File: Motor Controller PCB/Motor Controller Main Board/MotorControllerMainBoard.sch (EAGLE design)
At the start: 26 parts, among them T1 TEENSY_3.1_ALL_PINS

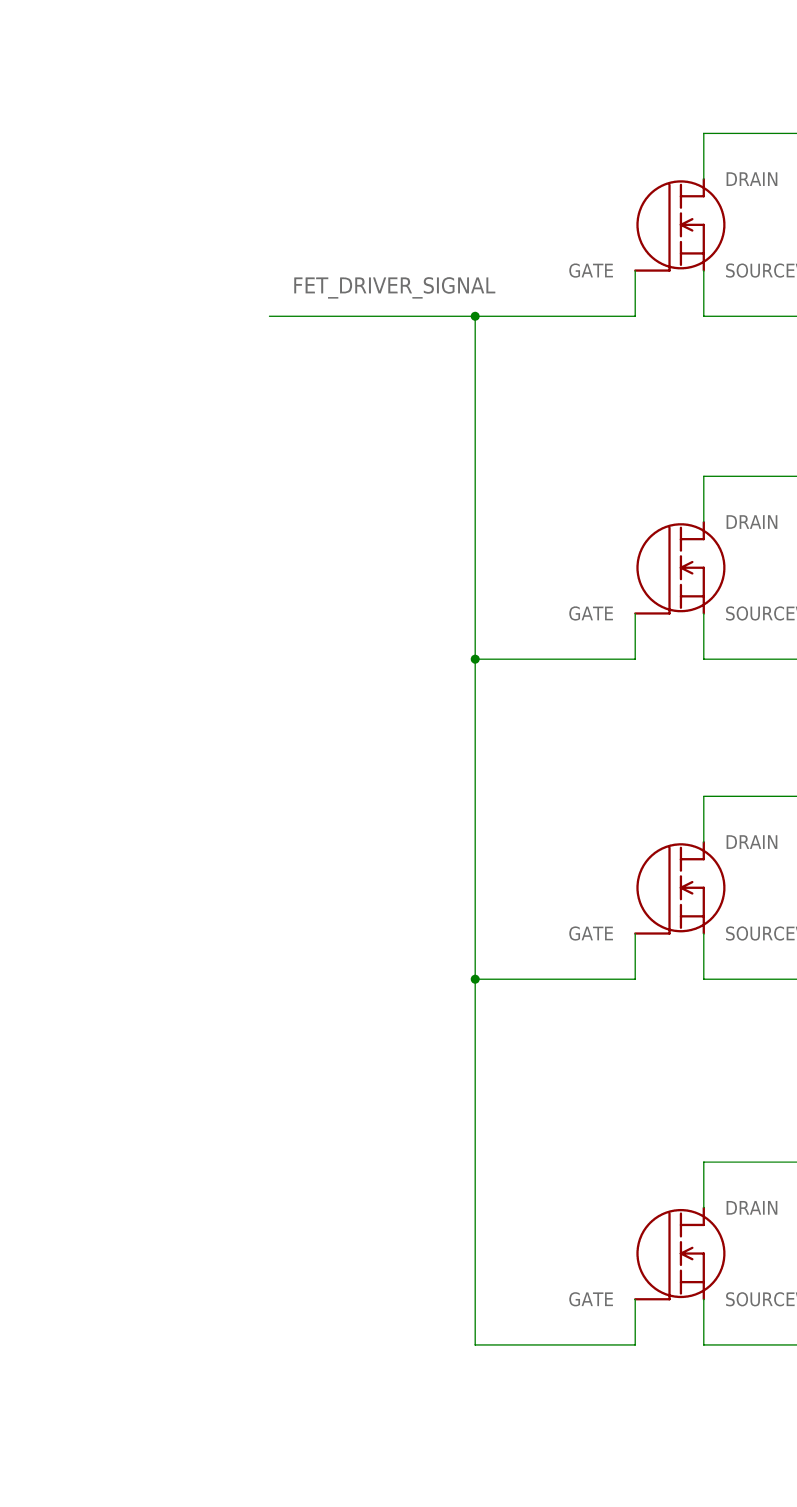
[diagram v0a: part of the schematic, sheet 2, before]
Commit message: Modified the mosfet network
added headers to enable/disable individual fets

also we're going to drive the fets with 12V instead of 15V.
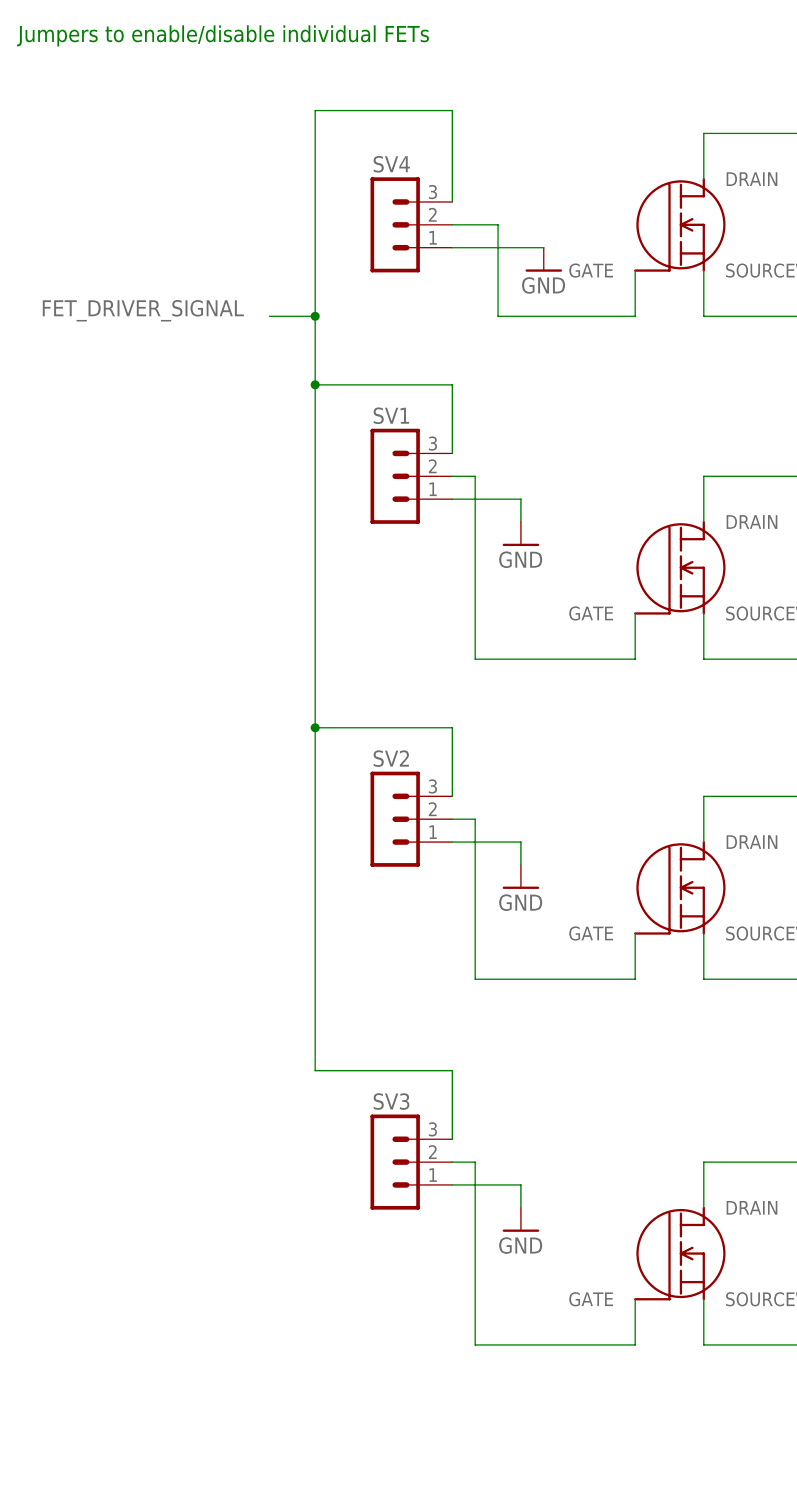
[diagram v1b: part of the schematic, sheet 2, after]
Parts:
- added SV1, SV2, SV3, SV4: (no value), con-lstb:MA03-1
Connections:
- net 15V_POWER_REGULATED renamed 12V_POWER_REGULATED
- new net N$3: SV1.2, U$2.GATE
- new net N$5: SV3.2, U$4.GATE
- new net N$8: SV4.2, U$1.GATE
- net FET_DRIVER_SIGNAL: now also SV1.3, SV2.2, SV2.3, SV3.3, SV4.3; no longer U$1.GATE, U$2.GATE, U$4.GATE
- net GND: now also SV1.1, SV2.1, SV3.1
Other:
- note added: "12V Variable Supply"
- note added: "Jumpers to enable/disable individual FETs"
- note removed: "15V Variable Supply"
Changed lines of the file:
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@@
 <?xml version="1.0" encoding="utf-8"?>
 <!DOCTYPE eagle SYSTEM "eagle.dtd">
-<eagle version="7.7.0">
+<eagle version="7.5.0">
 <drawing>
 <settings>
@@
 <part name="C12" library="MotorControllerEagleLibrary" deviceset="EEUFR1H221B" device=""/>
 <part name="U$13" library="MotorControllerEagleLibrary" deviceset="TL2575-05IKTTR" device=""/>
+<part name="SV1" library="con-lstb" deviceset="MA03-1" device=""/>
+<part name="SV2" library="con-lstb" deviceset="MA03-1" device=""/>
+<part name="SV3" library="con-lstb" deviceset="MA03-1" device=""/>
+<part name="GND5" library="E-P-008-R1.2" deviceset="GND" device=""/>
+<part name="GND6" library="E-P-008-R1.2" deviceset="GND" device=""/>
+<part name="GND7" library="E-P-008-R1.2" deviceset="GND" device=""/>
+<part name="SV4" library="con-lstb" deviceset="MA03-1" device=""/>
+<part name="GND8" library="E-P-008-R1.2" deviceset="GND" device=""/>
 </parts>
 <sheets>
@@
 </segment>
 </net>
-<net name="15V_POWER_REGULATED" class="0">
+<net name="12V_POWER_REGULATED" class="0">
 <segment>
 <wire x1="96.52" y1="66.04" x2="96.52" y2="58.42" width="0.1524" layer="91"/>
@@
 <plain>
 <text x="180.34" y="27.94" size="5.08" layer="94">POWER MOSFETS</text>
+<text x="63.5" y="195.58" size="1.778" layer="91">Jumpers to enable/disable individual FETs</text>
 </plain>
 <instances>
@@
 <instance part="U$4" gate="G$1" x="137.16" y="60.96"/>
 <instance part="GND2" gate="1" x="187.96" y="154.94"/>
+<instance part="SV1" gate="G$1" x="104.14" y="147.32"/>
+<instance part="SV2" gate="G$1" x="104.14" y="109.22"/>
+<instance part="SV3" gate="G$1" x="104.14" y="71.12"/>
+<instance part="GND5" gate="1" x="119.38" y="139.7"/>
+<instance part="GND6" gate="1" x="119.38" y="101.6"/>
+<instance part="GND7" gate="1" x="119.38" y="63.5"/>
+<instance part="SV4" gate="G$1" x="104.14" y="175.26"/>
+<instance part="GND8" gate="1" x="121.92" y="170.18"/>
 </instances>
 <busses>
@@
 <net name="FET_DRIVER_SIGNAL" class="0">
 <segment>
-<pinref part="U$1" gate="G$1" pin="GATE"/>
-<wire x1="132.08" y1="170.18" x2="132.08" y2="165.1" width="0.1524" layer="91"/>
-<wire x1="132.08" y1="165.1" x2="114.3" y2="165.1" width="0.1524" layer="91"/>
-<wire x1="114.3" y1="165.1" x2="114.3" y2="127" width="0.1524" layer="91"/>
-<pinref part="U$2" gate="G$1" pin="GATE"/>
-<wire x1="114.3" y1="127" x2="132.08" y2="127" width="0.1524" layer="91"/>
-<wire x1="132.08" y1="127" x2="132.08" y2="132.08" width="0.1524" layer="91"/>
-<wire x1="114.3" y1="127" x2="114.3" y2="91.44" width="0.1524" layer="91"/>
-<junction x="114.3" y="127"/>
 <pinref part="U$3" gate="G$1" pin="GATE"/>
 <wire x1="114.3" y1="91.44" x2="132.08" y2="91.44" width="0.1524" layer="91"/>
 <wire x1="132.08" y1="91.44" x2="132.08" y2="96.52" width="0.1524" layer="91"/>
-<wire x1="114.3" y1="91.44" x2="114.3" y2="50.8" width="0.1524" layer="91"/>
-<junction x="114.3" y="91.44"/>
-<pinref part="U$4" gate="G$1" pin="GATE"/>
-<wire x1="114.3" y1="50.8" x2="132.08" y2="50.8" width="0.1524" layer="91"/>
-<wire x1="132.08" y1="50.8" x2="132.08" y2="55.88" width="0.1524" layer="91"/>
-<wire x1="114.3" y1="165.1" x2="91.44" y2="165.1" width="0.1524" layer="91"/>
-<junction x="114.3" y="165.1"/>
-<label x="93.98" y="167.64" size="1.778" layer="95"/>
+<pinref part="SV2" gate="G$1" pin="2"/>
+<wire x1="111.76" y1="109.22" x2="114.3" y2="109.22" width="0.1524" layer="91"/>
+<wire x1="114.3" y1="109.22" x2="114.3" y2="91.44" width="0.1524" layer="91"/>
+</segment>
+<segment>
+<label x="66.04" y="165.1" size="1.778" layer="95"/>
+<wire x1="96.52" y1="165.1" x2="91.44" y2="165.1" width="0.1524" layer="91"/>
+<wire x1="96.52" y1="165.1" x2="96.52" y2="157.48" width="0.1524" layer="91"/>
+<pinref part="SV1" gate="G$1" pin="3"/>
+<wire x1="96.52" y1="157.48" x2="111.76" y2="157.48" width="0.1524" layer="91"/>
+<wire x1="111.76" y1="157.48" x2="111.76" y2="149.86" width="0.1524" layer="91"/>
+<wire x1="96.52" y1="157.48" x2="96.52" y2="119.38" width="0.1524" layer="91"/>
+<junction x="96.52" y="157.48"/>
+<pinref part="SV2" gate="G$1" pin="3"/>
+<wire x1="96.52" y1="119.38" x2="111.76" y2="119.38" width="0.1524" layer="91"/>
+<wire x1="111.76" y1="119.38" x2="111.76" y2="111.76" width="0.1524" layer="91"/>
+<wire x1="96.52" y1="119.38" x2="96.52" y2="81.28" width="0.1524" layer="91"/>
+<junction x="96.52" y="119.38"/>
+<pinref part="SV3" gate="G$1" pin="3"/>
+<wire x1="96.52" y1="81.28" x2="111.76" y2="81.28" width="0.1524" layer="91"/>
+<wire x1="111.76" y1="81.28" x2="111.76" y2="73.66" width="0.1524" layer="91"/>
+<wire x1="96.52" y1="165.1" x2="96.52" y2="187.96" width="0.1524" layer="91"/>
+<junction x="96.52" y="165.1"/>
+<pinref part="SV4" gate="G$1" pin="3"/>
+<wire x1="96.52" y1="187.96" x2="111.76" y2="187.96" width="0.1524" layer="91"/>
+<wire x1="111.76" y1="187.96" x2="111.76" y2="177.8" width="0.1524" layer="91"/>
 </segment>
 </net>
@@
 <wire x1="187.96" y1="165.1" x2="187.96" y2="157.48" width="0.1524" layer="91"/>
 <label x="177.8" y="167.64" size="1.778" layer="95"/>
+</segment>
+<segment>
+<pinref part="SV1" gate="G$1" pin="1"/>
+<wire x1="111.76" y1="144.78" x2="119.38" y2="144.78" width="0.1524" layer="91"/>
+<wire x1="119.38" y1="144.78" x2="119.38" y2="142.24" width="0.1524" layer="91"/>
+<pinref part="GND5" gate="1" pin="GND"/>
+</segment>
+<segment>
+<pinref part="SV2" gate="G$1" pin="1"/>
+<wire x1="111.76" y1="106.68" x2="119.38" y2="106.68" width="0.1524" layer="91"/>
+<wire x1="119.38" y1="106.68" x2="119.38" y2="104.14" width="0.1524" layer="91"/>
+<pinref part="GND6" gate="1" pin="GND"/>
+</segment>
+<segment>
+<pinref part="SV3" gate="G$1" pin="1"/>
+<wire x1="111.76" y1="68.58" x2="119.38" y2="68.58" width="0.1524" layer="91"/>
+<wire x1="119.38" y1="68.58" x2="119.38" y2="66.04" width="0.1524" layer="91"/>
+<pinref part="GND7" gate="1" pin="GND"/>
+</segment>
+<segment>
+<wire x1="111.76" y1="172.72" x2="121.92" y2="172.72" width="0.1524" layer="91"/>
+<pinref part="GND8" gate="1" pin="GND"/>
+</segment>
+</net>
+<net name="N$3" class="0">
+<segment>
+<pinref part="U$2" gate="G$1" pin="GATE"/>
+<wire x1="114.3" y1="127" x2="132.08" y2="127" width="0.1524" layer="91"/>
+<wire x1="132.08" y1="127" x2="132.08" y2="132.08" width="0.1524" layer="91"/>
+<pinref part="SV1" gate="G$1" pin="2"/>
+<wire x1="111.76" y1="147.32" x2="114.3" y2="147.32" width="0.1524" layer="91"/>
+<wire x1="114.3" y1="147.32" x2="114.3" y2="127" width="0.1524" layer="91"/>
+</segment>
+</net>
+<net name="N$5" class="0">
+<segment>
+<pinref part="U$4" gate="G$1" pin="GATE"/>
+<wire x1="132.08" y1="50.8" x2="132.08" y2="55.88" width="0.1524" layer="91"/>
+<wire x1="114.3" y1="50.8" x2="132.08" y2="50.8" width="0.1524" layer="91"/>
+<pinref part="SV3" gate="G$1" pin="2"/>
+<wire x1="111.76" y1="71.12" x2="114.3" y2="71.12" width="0.1524" layer="91"/>
+<wire x1="114.3" y1="71.12" x2="114.3" y2="50.8" width="0.1524" layer="91"/>
+</segment>
+</net>
+<net name="N$8" class="0">
+<segment>
+<pinref part="U$1" gate="G$1" pin="GATE"/>
+<wire x1="132.08" y1="170.18" x2="132.08" y2="165.1" width="0.1524" layer="91"/>
+<pinref part="SV4" gate="G$1" pin="2"/>
+<wire x1="111.76" y1="175.26" x2="116.84" y2="175.26" width="0.1524" layer="91"/>
+<wire x1="116.84" y1="175.26" x2="116.84" y2="165.1" width="0.1524" layer="91"/>
+<wire x1="116.84" y1="165.1" x2="132.08" y2="165.1" width="0.1524" layer="91"/>
 </segment>
 </net>
@@
 </busses>
 <nets>
-<net name="15V_POWER_REGULATED" class="0">
+<net name="12V_POWER_REGULATED" class="0">
 <segment>
 <pinref part="MIC4452" gate="G$1" pin="VS"/>
@@
 <plain>
 <text x="200.66" y="27.94" size="3.81" layer="94">POWER SUPPLY</text>
-<text x="172.72" y="154.94" size="6.4516" layer="94">15V Variable Supply</text>
+<text x="172.72" y="154.94" size="6.4516" layer="94">12V Variable Supply</text>
 <text x="172.72" y="83.82" size="6.4516" layer="94">5V Supply</text>
 <text x="58.42" y="149.86" size="1.27" layer="94">220uF Panasonic Caps</text>
@@
 </segment>
 </net>
-<net name="15V_POWER_REGULATED" class="0">
+<net name="12V_POWER_REGULATED" class="0">
 <segment>
 <pinref part="C8" gate="A" pin="11"/>

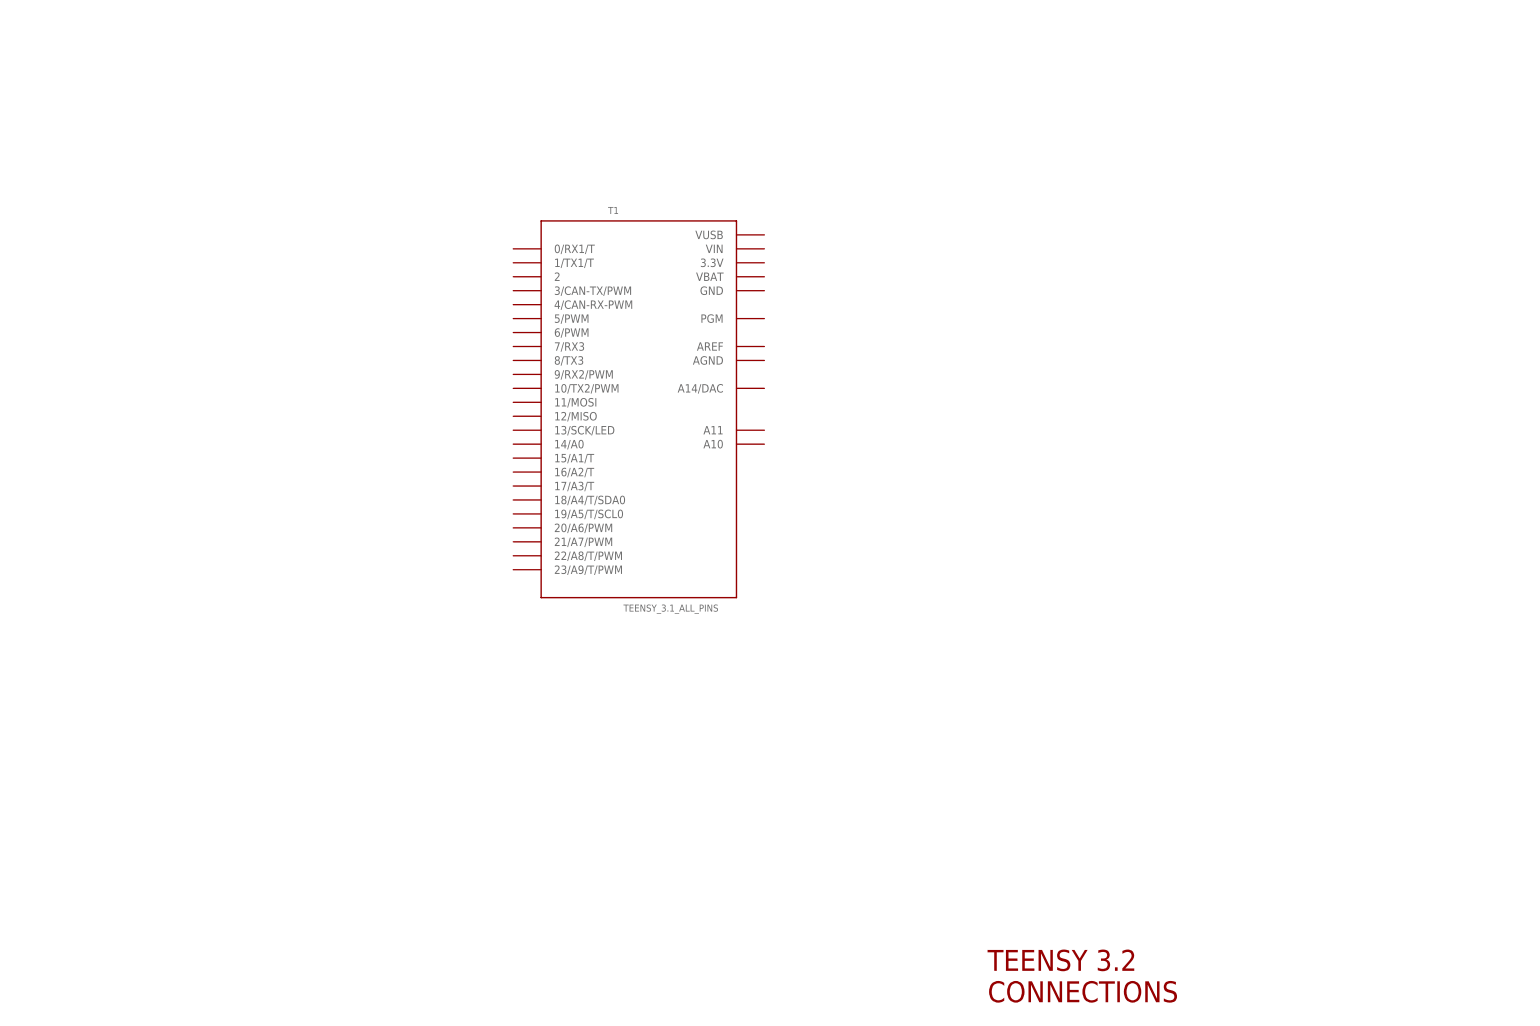
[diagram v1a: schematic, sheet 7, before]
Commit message: Added Teensy Pins
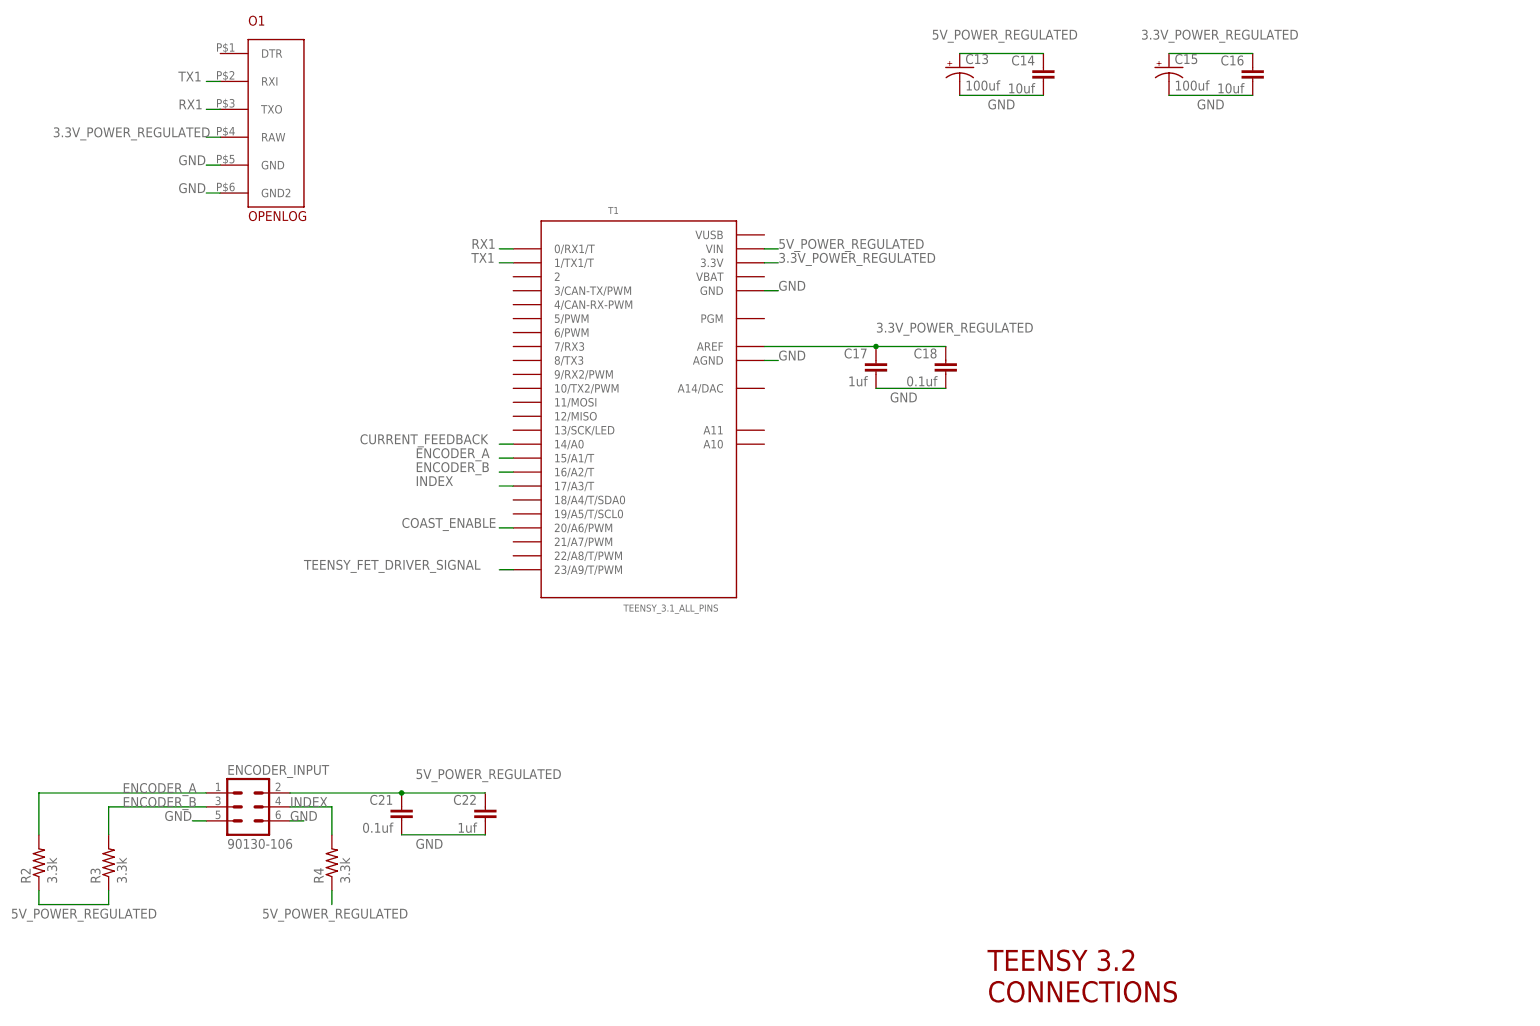
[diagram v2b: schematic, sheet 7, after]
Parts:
- added C13, C15: 100uf, SparkFun-Capacitors:CAP_POLC
- added C14, C16: 10uf, SparkFun-Capacitors:CAP0805
- added C17, C19, C22: 1uf, SparkFun-Capacitors:CAP0805
- added C18, C20, C21: 0.1uf, SparkFun-Capacitors:CAP0805
- added ENCODER_INPUT: 90130-106, con-molex-c-grid:90130-106
- added O1: OPENLOG, openlog:OPENLOG
- added R2, R3, R4: 3.3k, SparkFun-Passives:RESISTOR0805-RES
- added U$9: (no value), MotorControllerEagleLibrary:PA4320
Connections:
- new net 3.3V_POWER_REGULATED: C15.+, C16.1, C17.1, C18.1, C19.1, C20.1, O1.RAW, T1.3.3V, T1.AREF, U$9.-
- new net COAST_ENABLE: T1.20/A6/PWM
- new net CURRENT_FEEDBACK: T1.14/A0
- new net ENCODER_A: ENCODER_INPUT.1, R2.2, T1.15/A1/T
- new net ENCODER_B: ENCODER_INPUT.3, R3.2, T1.16/A2/T
- new net INDEX: ENCODER_INPUT.4, R4.2, T1.17/A3/T
- new net N$6: U$9.+
- new net RX1: O1.TXO, T1.0/RX1/T
- new net TX1: O1.RXI, T1.1/TX1/T
- net 5V_POWER_REGULATED: now also C13.+, C14.1, C21.1, C22.1, ENCODER_INPUT.2, R2.1, R3.1, R4.1, T1.VIN
- net GND: now also C13.-, C14.2, C15.-, C16.2, C17.2, C18.2, C19.2, C20.2, C21.2, C22.2, ENCODER_INPUT.5, ENCODER_INPUT.6, O1.GND, O1.GND2, T1.AGND, T1.GND
- net TEENSY_FET_DRIVER_SIGNAL: now also T1.23/A9/T/PWM
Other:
- note added: "INSERT CURRENT SENSOR HERE"
